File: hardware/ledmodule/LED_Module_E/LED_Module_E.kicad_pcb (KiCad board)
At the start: 4 copper layers, 140.8 x 26 mm, 93 parts, among them J1 SFW20S-2STE1LF, J3 009159008603906, Q1 Si3456DDV, Q11 Si3456DDV, Q12 Si3456DDV, Q2 Si3456DDV, Q3 Si3456DDV, Q4 Si3456DDV, Q5 Si3456DDV, Q6 Si3456DDV, Q7 Si3456DDV, Q8 Si3456DDV, U1 TMP1075DGK, U2 74HCT244, U3 24AA02UIDT-I/OT

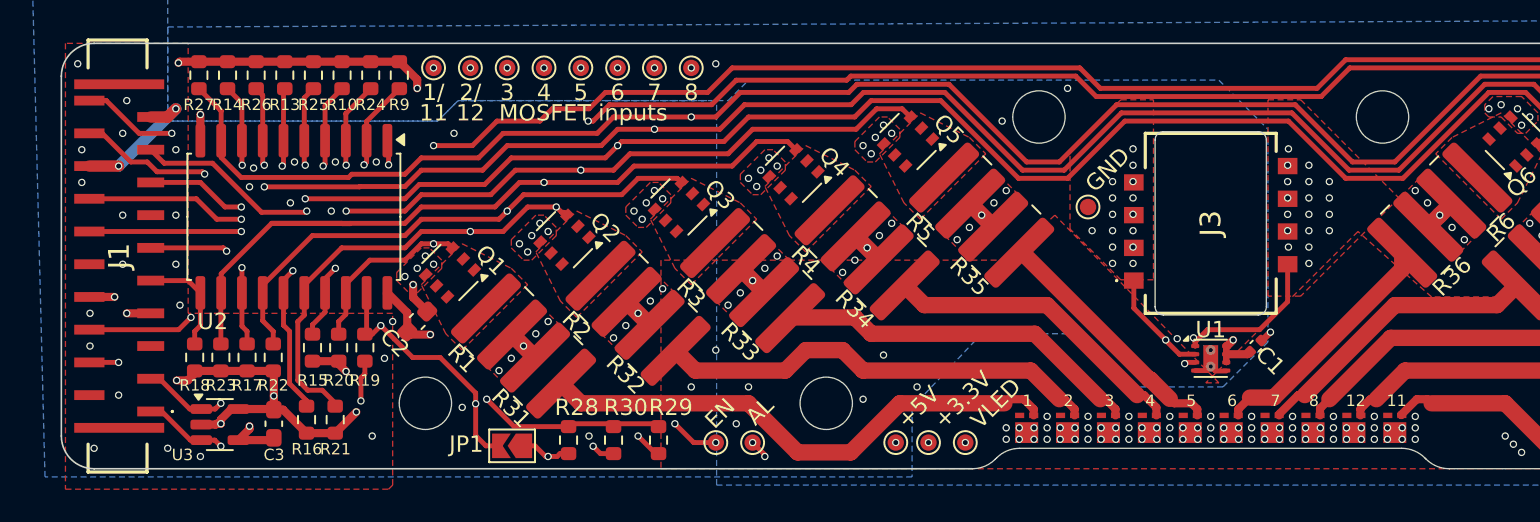
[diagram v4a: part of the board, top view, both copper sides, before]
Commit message: Latest versions of all five PCBs that make up the ABL, maybe ready for prototype production.
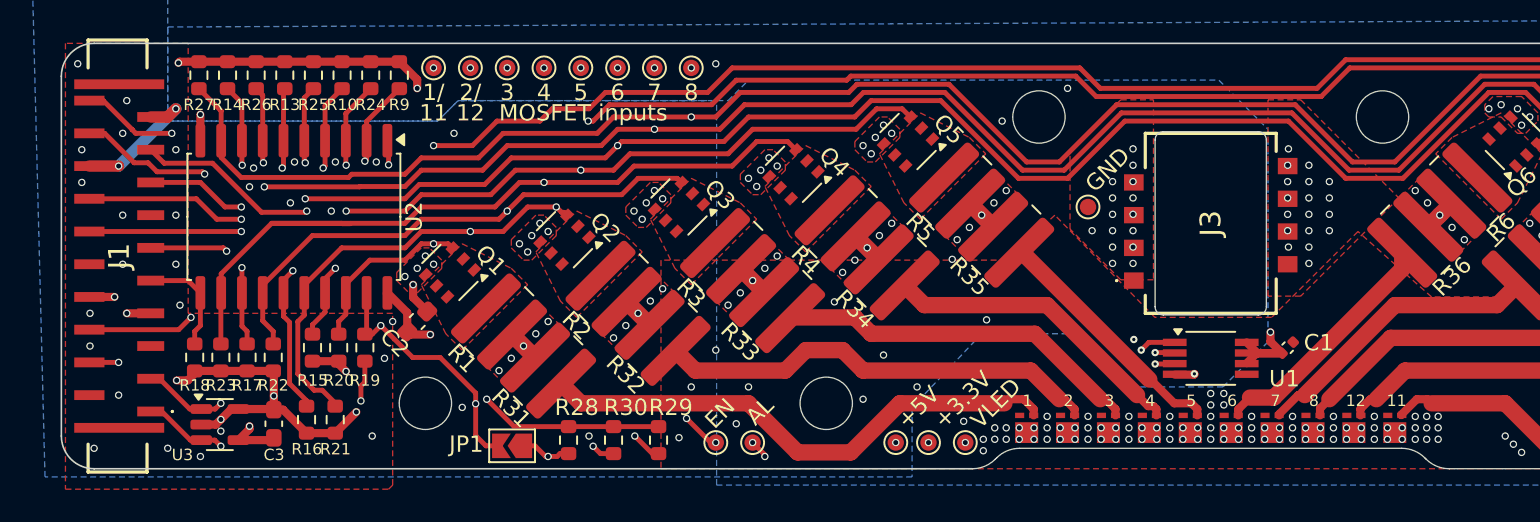
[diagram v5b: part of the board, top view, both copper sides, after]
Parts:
- U1: footprint Package_SON:WSON-8-1EP_2x2mm_P0.5mm_EP0.9x1.6mm_ThermalVias -> Package_SO:VSSOP-8_3.0x3.0mm_P0.65mm
- moved C1 1.95 mm to (142.2, 75.6)
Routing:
- net /SDA: track 82.7 -> 71.6 mm
- net /SCL: track 78.7 -> 73.4 mm
- net +3.3V: track 115.5 -> 120.6 mm
- net GND: track 44.4 -> 42.6 mm, vias 137 -> 142
- net /ALERT: track 78.2 -> 76.7 mm
- net /i1: track 22.6 -> 23.4 mm
- net Net-(Q5-G): track 51.7 -> 52.4 mm
- net +4V: vias 128 -> 143
- added copper zone on In2.Cu, net Net-(R1-Pad1)
- added copper zone on In2.Cu, net Net-(R2-Pad1)
- added copper zone on In2.Cu, net Net-(R3-Pad1)
- added copper zone on In2.Cu, net Net-(R34-Pad2)
- added copper zone on In2.Cu, net Net-(R35-Pad2)

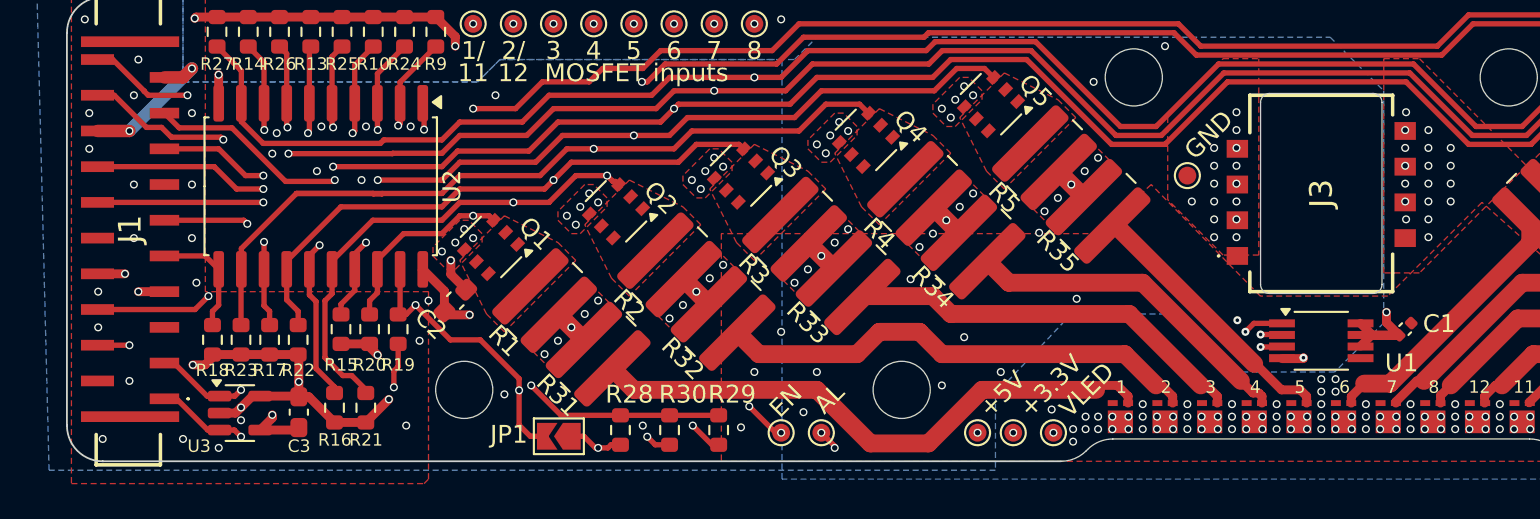
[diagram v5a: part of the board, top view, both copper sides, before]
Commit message: Clean up schematics and minor fixes in PCB layouts.
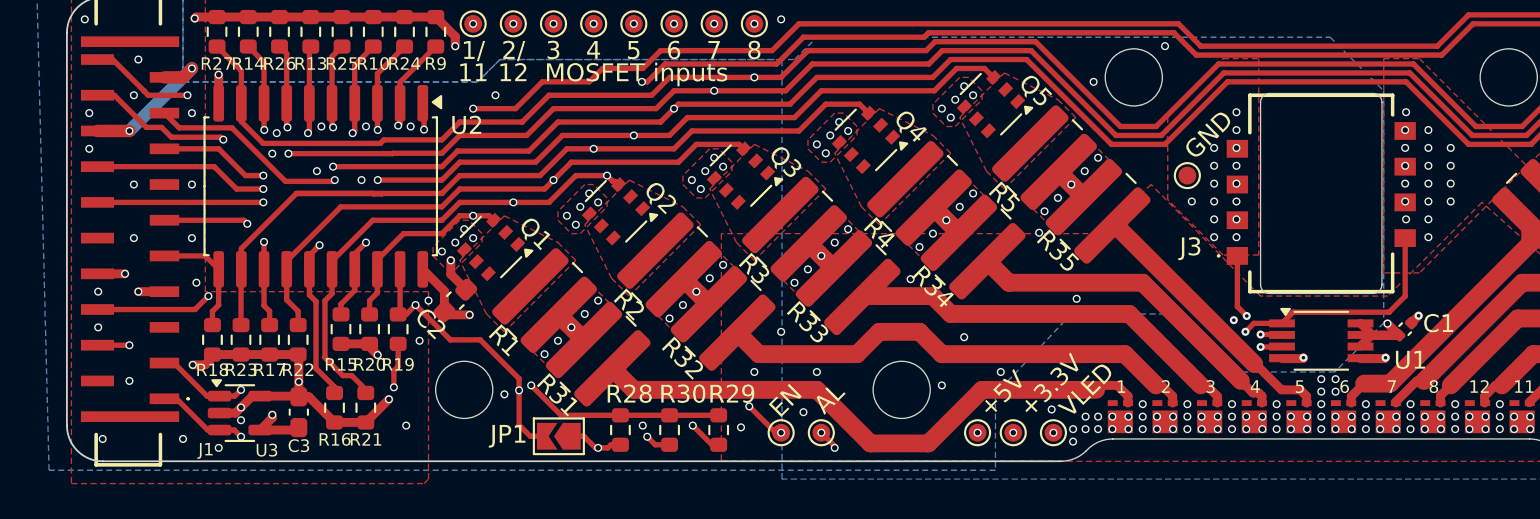
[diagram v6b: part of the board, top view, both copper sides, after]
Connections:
- J3 pad 4: +4V -> +5V
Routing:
- net +5V: track 59.2 -> 111.6 mm, vias 4 -> 5
- net /SDA: track 71.6 -> 82.4 mm
- net /SCL: track 73.4 -> 76.9 mm, vias 3 -> 4
- net GND: track 42.6 -> 44.6 mm, vias 142 -> 144
- net +4V: vias 143 -> 142
